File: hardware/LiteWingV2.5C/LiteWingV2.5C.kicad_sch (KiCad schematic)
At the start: 87 parts, among them IC1 TP4056, J1 USB_C_Receptacle_USB2.0, J10 Conn_01x02_Female, J11 Conn_01x09, J12 Conn_01x06, J13 Conn_01x07, J14 Conn_01x02, J2 JST XH 2P 2.50mm SMD Hoz, J3 Conn_01x06, J4 Conn_01x06, J5 Conn_01x06, J6 Conn_01x06, J7 Conn_01x02_Female, J8 Conn_01x02_Female, J9 Conn_01x02_Female, SW1 MST22D18G2_125, SW2 Tactile Switch 3x4x2, SW3 Tactile Switch 3x4x2, T1 IRLML6344TRPBF, T2 IRLML6344TRPBF, T3 IRLML6344TRPBF, T4 IRLML6344TRPBF, U1 AO3401A, U2 SPX3819M5-L-3-3/TR, U5 CH340K, U6 2N27002DW, U7 MPU-6050, U8 ESP32-S3-WROOM-1

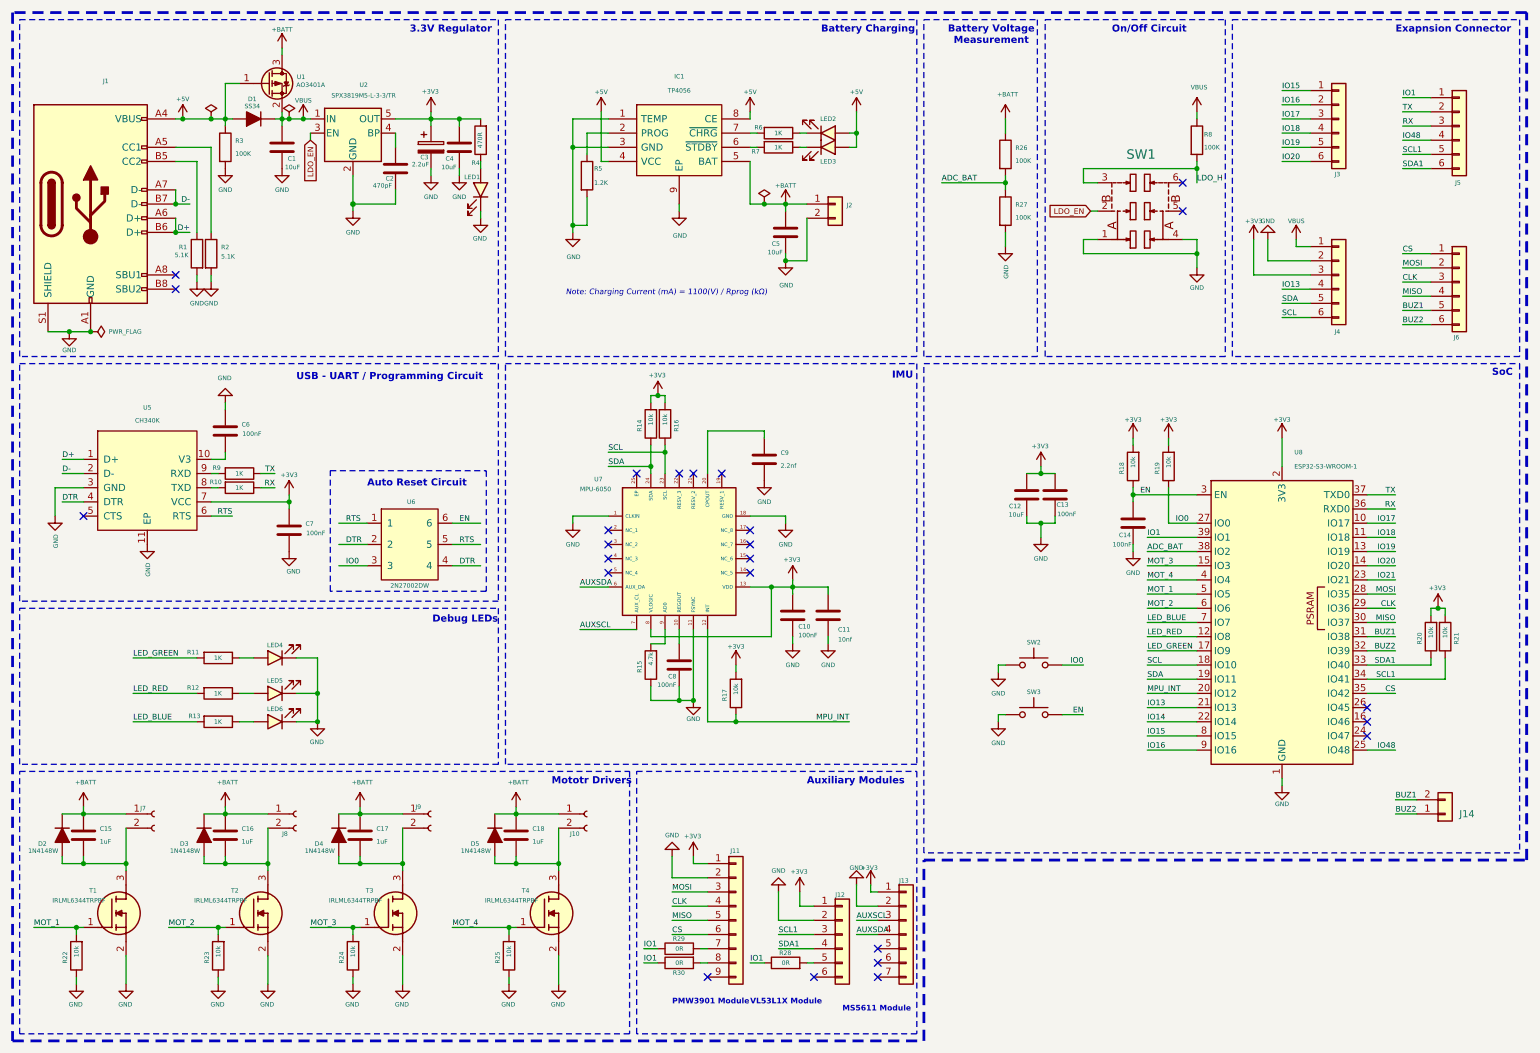
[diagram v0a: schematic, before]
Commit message: Fixed spelling errors. Moved DroneV2 footprints into the repo instead of referencing the engineer's filesystem which lies outside of git source control.
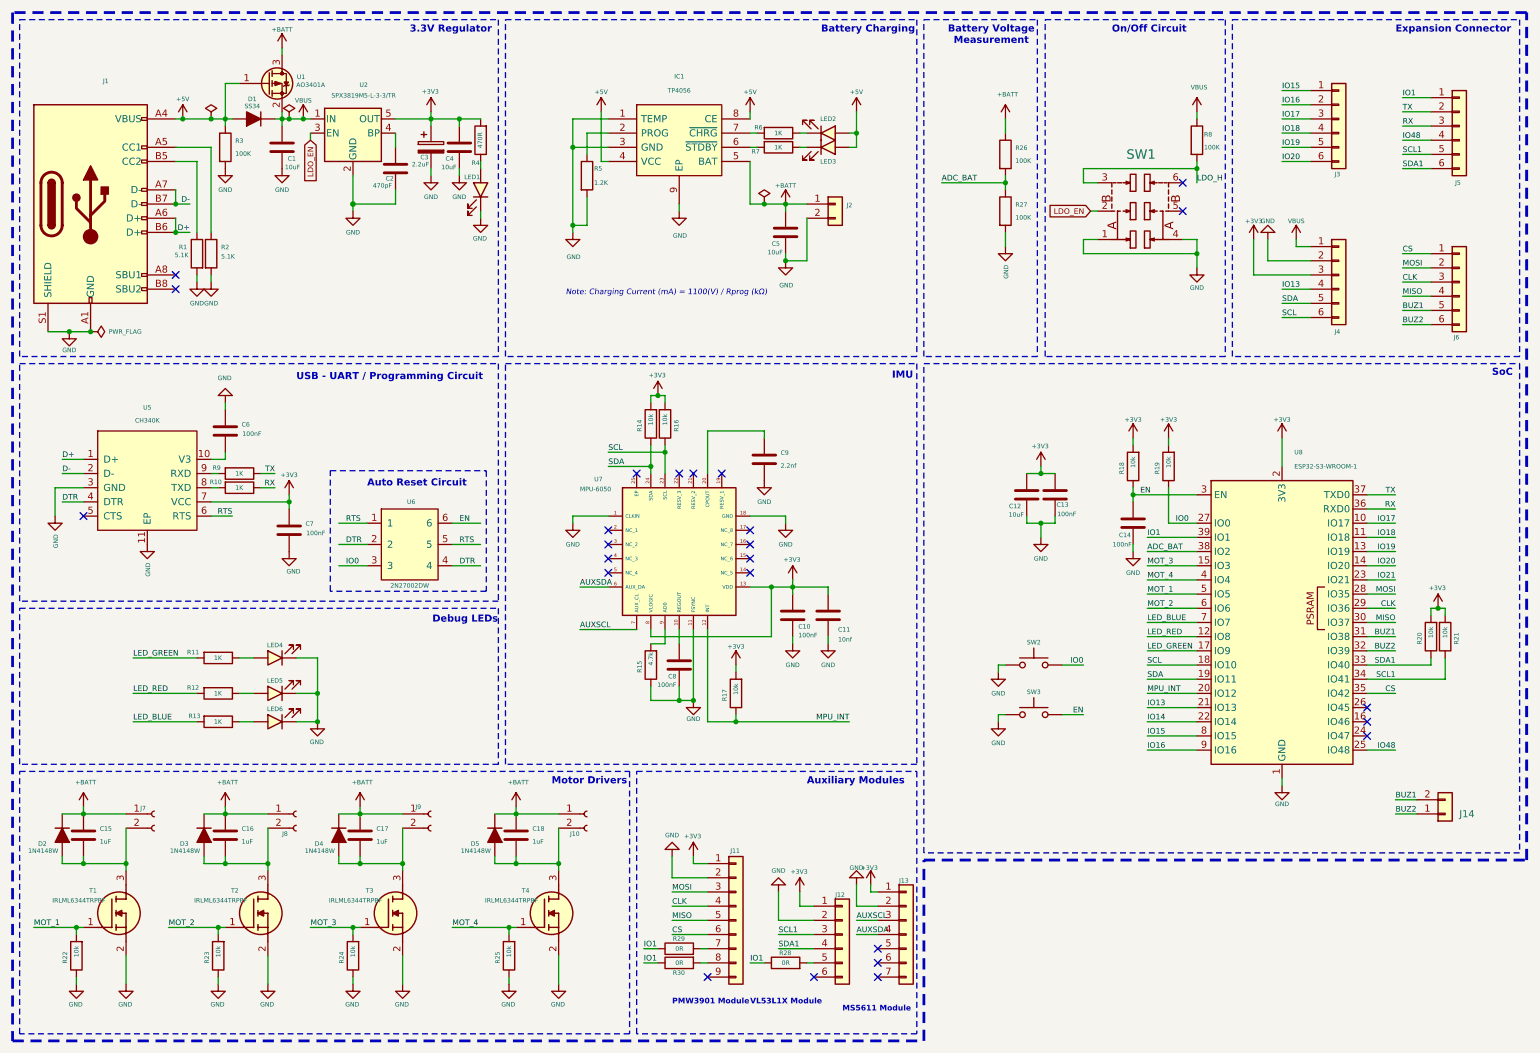
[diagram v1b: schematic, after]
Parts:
- IC1: footprint tp4056:SOIC127P600X175-9N -> DroneV2:SOIC127P600X175-9N
- J14: footprint ConnTH1.25MM:CONN-TH_1.25T-2A_1.25T-2A -> DroneV2:CONN-TH_1.25T-2A_1.25T-2A
- J2: footprint XH2P:CONN-TH_2P-P2.50_XH-2AW -> DroneV2:CONN-TH_2P-P2.50_XH-2AW
- SW1: footprint SlideSwitchSMDTop:SW-SMD_MST22D18G2 -> DroneV2:SW-SMD_MST22D18G2
- SW2, SW3: footprint 3x4x2:Tactile 3x4x2mm TS-A010 -> DroneV2:Tactile 3x4x2mm TS-A010
- T1, T2, T3, T4: footprint SI2302DS-T1:SOT95P237X112-3N -> DroneV2:SOT95P237X112-3N
- U5: footprint ch340k:ESSOP-10_3.9x4.9mm_P1.00mm -> DroneV2:ESSOP-10_3.9x4.9mm_P1.00mm
- U7: footprint MPU6050:MPU6050 -> DroneV2:MPU6050
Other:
- note added: "Expansion Connector"
- note added: "Motor Drivers"
- note removed: "Exapnsion Connector"
- note removed: "Mototr Drivers"
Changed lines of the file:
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@@
 		)
 	)
-	(text "Mototr Drivers"
+	(text "Motor Drivers"
 		(exclude_from_sim no)
 		(at 109.22 151.13 0)
@@
 		)
 	)
-	(text "Exapnsion Connector"
+	(text "Expansion Connector"
 		(exclude_from_sim no)
 		(at 260.35 16.51 0)
@@
 			)
 		)
-		(property "Footprint" "SI2302DS-T1:SOT95P237X112-3N"
+		(property "Footprint" "DroneV2:SOT95P237X112-3N"
 			(at 25.4 176.53 0)
 			(effects
@@
 			)
 		)
-		(property "Footprint" "SI2302DS-T1:SOT95P237X112-3N"
+		(property "Footprint" "DroneV2:SOT95P237X112-3N"
 			(at 50.8 176.53 0)
 			(effects
@@
 			)
 		)
-		(property "Footprint" "ch340k:ESSOP-10_3.9x4.9mm_P1.00mm"
+		(property "Footprint" "DroneV2:ESSOP-10_3.9x4.9mm_P1.00mm"
 			(at 36.83 96.52 0)
 			(effects
@@
 			)
 		)
-		(property "Footprint" "MPU6050:MPU6050"
+		(property "Footprint" "DroneV2:MPU6050"
 			(at 112.014 100.584 0)
 			(effects
@@
 			)
 		)
-		(property "Footprint" "SlideSwitchSMDTop:SW-SMD_MST22D18G2"
+		(property "Footprint" "DroneV2:SW-SMD_MST22D18G2"
 			(at 214.63 48.26 0)
 			(effects
@@
 			)
 		)
-		(property "Footprint" "ConnTH1.25MM:CONN-TH_1.25T-2A_1.25T-2A"
+		(property "Footprint" "DroneV2:CONN-TH_1.25T-2A_1.25T-2A"
 			(at 269.24 156.21 0)
 			(effects
@@
 			)
 		)
-		(property "Footprint" "SI2302DS-T1:SOT95P237X112-3N"
+		(property "Footprint" "DroneV2:SOT95P237X112-3N"
 			(at 102.87 176.53 0)
 			(effects
@@
 			)
 		)
-		(property "Footprint" "SI2302DS-T1:SOT95P237X112-3N"
+		(property "Footprint" "DroneV2:SOT95P237X112-3N"
 			(at 74.93 176.53 0)
 			(effects
@@
 			)
 		)
-		(property "Footprint" "XH2P:CONN-TH_2P-P2.50_XH-2AW"
+		(property "Footprint" "DroneV2:CONN-TH_2P-P2.50_XH-2AW"
 			(at 161.036 43.688 0)
 			(effects
@@
 			)
 		)
-		(property "Footprint" "3x4x2:Tactile 3x4x2mm TS-A010"
+		(property "Footprint" "DroneV2:Tactile 3x4x2mm TS-A010"
 			(at 195.58 133.35 0)
 			(effects
@@
 			)
 		)
-		(property "Footprint" "tp4056:SOIC127P600X175-9N"
+		(property "Footprint" "DroneV2:SOIC127P600X175-9N"
 			(at 143.51 29.21 0)
 			(effects
@@
 			)
 		)
-		(property "Footprint" "3x4x2:Tactile 3x4x2mm TS-A010"
+		(property "Footprint" "DroneV2:Tactile 3x4x2mm TS-A010"
 			(at 195.58 124.46 0)
 			(effects
